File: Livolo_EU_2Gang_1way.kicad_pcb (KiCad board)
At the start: 2 copper layers, 43 x 43 mm, 54 parts, among them IC1 ATMEGA328P, U1 ATSHA204A, U2 NRF24L01, U3 MIC5205-3.3, U4 MCP16301, U5 AT25DF512C

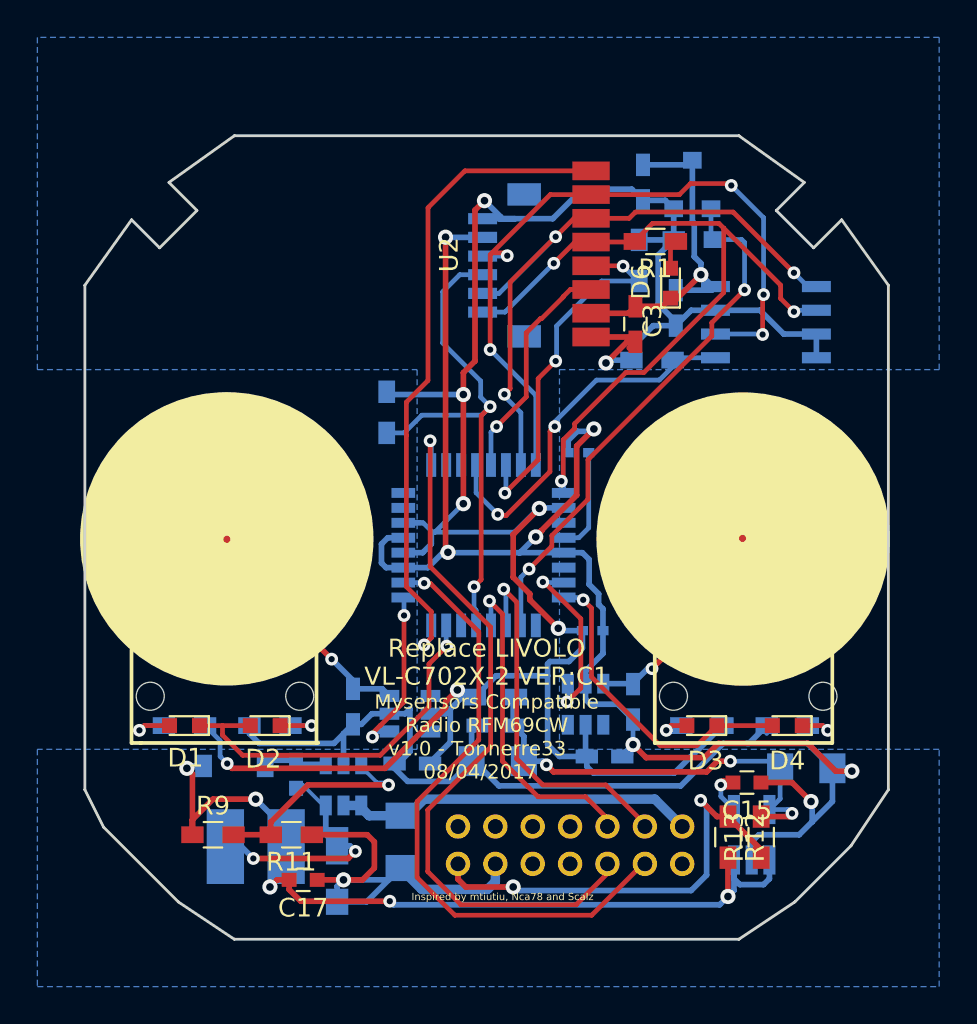
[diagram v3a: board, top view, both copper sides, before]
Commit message: replace TTP223 by MTCH105
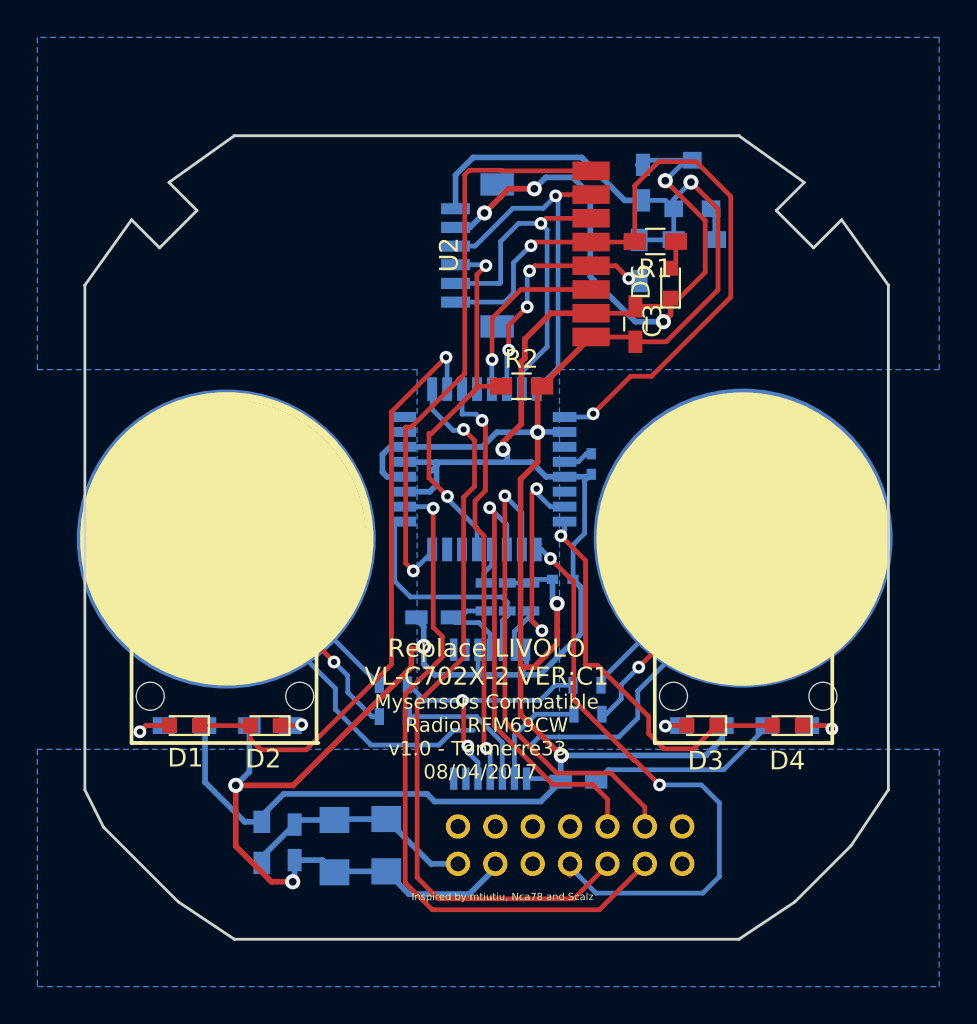
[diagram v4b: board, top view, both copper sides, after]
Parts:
- removed C11: 10u/25v, Livolo_EU_2Gang_1way:EIA3216
- removed C14, C7, C9: 100n, Capacitors_SMD:C_0603_HandSoldering
- removed C15: 470p, Capacitors_SMD:C_0603
- removed C16: 100n, Capacitors_SMD:C_0603
- removed C17: 22u, Capacitors_SMD:C_0603
- removed C8: 0-50pF, Capacitors_SMD:C_0603_HandSoldering
- removed D5: SS14M, Livolo:SS14M
- removed D7: 1N4148, Diodes_SMD:D_SOD-123
- removed L1: 15uH, Livolo:VLCF4020T-150MR68
- removed R10: 56k, Resistors_SMD:R_0603_HandSoldering
- removed R11: 10k, Resistors_SMD:R_0603_HandSoldering
- removed R12, R13: *1, Resistors_SMD:R_0603_HandSoldering
- removed R9: 31k6, Resistors_SMD:R_0603_HandSoldering
- removed U$1, U$5: SENSOR_PAD_ROUND, Livolo:touch_pad_16mm
- removed U$4, U$6: TTP223-BA6, TO_SOT_Packages_SMD:SOT-23-6
- removed U3: MIC5205-3.3, TO_SOT_Packages_SMD:SOT-23-5_HandSoldering
- removed U4: MCP16301, TO_SOT_Packages_SMD:SOT-23-6
- removed U5: AT25DF512C, Housings_SOIC:SOIC-8_3.9x4.9mm_Pitch1.27mm
- added C1: 100n, Capacitors_SMD:C_0603_HandSoldering, B.Cu at (153.4, 118.1)
- added R14: 4K7, Resistors_SMD:R_0603, B.Cu at (143.5, 114.6)
- added R15: 0, Resistors_SMD:R_0603, B.Cu at (143.5, 112.9)
- added R16: 4K7, Resistors_SMD:R_0603, B.Cu at (153.9, 114.5)
- added R17: 0, Resistors_SMD:R_0603, B.Cu at (153.9, 112.9)
- added R18: 10K, Resistors_SMD:R_0603, B.Cu at (150.9, 108.2)
- added R19: 10K, Resistors_SMD:R_0603, B.Cu at (148.4, 108.2)
- added R20: 10K, Resistors_SMD:R_0603, B.Cu at (149.6, 108.2)
- added U6: Touch, Livolo:livolo_ts_guard, B.Cu at (134.6, 105.1)
- added U7: Touch, Livolo:livolo_ts_guard, B.Cu at (162.2, 105.0)
- added U8: MTCH105, Housings_SSOP:SSOP-14_5.3x6.2mm_Pitch0.65mm, B.Cu at (148.7, 114.5)
- C4: value 0-50pF -> 1uF
- R2: moved to F.Cu
- moved C12 25.6 mm to (140.4, 121.5), turned to 90 degrees
- moved L2 14.7 mm to (136.5, 121.3), turned to 270 degrees
- moved C13 12.4 mm to (138.2, 121.3), turned to 270 degrees
- moved C4 11.6 mm to (145.7, 109.3), turned to 180 degrees
- moved C10 7.47 mm to (143.1, 121.5), turned to 90 degrees
- moved R2 7.35 mm to (150.4, 96.9), turned to 0 degrees
- moved IC1 4.06 mm to (148.4, 101.4)
- moved C6 3.18 mm to (152.6, 107.2)
- moved SL2 1.54 mm to (148.1, 89.9)
- moved C2 0.92 mm to (154.1, 101.1), turned to 90 degrees
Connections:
- C10 pad +: Net-(C10-Pad+) -> /3.3VCC-Liv
- C12 pad +: Net-(C10-Pad+) -> /3.3VCC-Liv
- C13 pad 1: Net-(C10-Pad+) -> /3.3VCC-Liv
- C4 pad 1: GND -> Net-(C4-Pad1)
- C4 pad 2: Net-(C4-Pad2) -> GND
- IC1 pad 10: (no net) -> /LED1
- IC1 pad 11: (no net) -> /MTPM
- IC1 pad 12: /FLASH_CS -> (no net)
- IC1 pad 25: (no net) -> /BUZZER
- IC1 pad 26: /A3_ATSHA -> /L2_SET
- IC1 pad 27: /L2_SET -> /L2_RST
- IC1 pad 28: /L2_RST -> /MTSA
- IC1 pad 31: /LED1 -> (no net)
- L2 pad 2: Net-(C10-Pad+) -> /3.3VCC-Liv
- U$2 pad 13: /+12VCC -> (no net)
- U$2 pad 8: (no net) -> /BUZZER
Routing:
- net /3.3VCC_1: track 49.1 -> 0.00 mm, vias 5 -> 0
- net GND: track 174.9 -> 134.8 mm, vias 9 -> 8
- net Net-(R15-Pad2): track 0.00 -> 33.6 mm
- net /BUZZER: track 0.00 -> 32.8 mm, vias 0 -> 2
- net Net-(R17-Pad2): track 0.00 -> 31.9 mm
- net /A3_ATSHA: track 28.8 -> 1.73 mm, vias 2 -> 0
- net Net-(C10-Pad+): track 24.5 -> 0.00 mm, vias 3 -> 0
- net /MTPM: track 0.00 -> 22.4 mm, vias 0 -> 2
- net /+12VCC: track 20.5 -> 0.00 mm
- net /MISO: track 40.5 -> 20.2 mm, vias 5 -> 1
- net /FLASH_CS: track 19.9 -> 0.00 mm, vias 2 -> 0
- net VCC: track 135.7 -> 118.1 mm, vias 8 -> 4
- net /MOSI: track 35.0 -> 20.5 mm, vias 3 -> 1
- net Net-(R15-Pad1): track 0.00 -> 14.1 mm, vias 0 -> 2
- net Net-(R14-Pad2): track 0.00 -> 13.1 mm, vias 0 -> 1
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
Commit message: ajust silkscreen
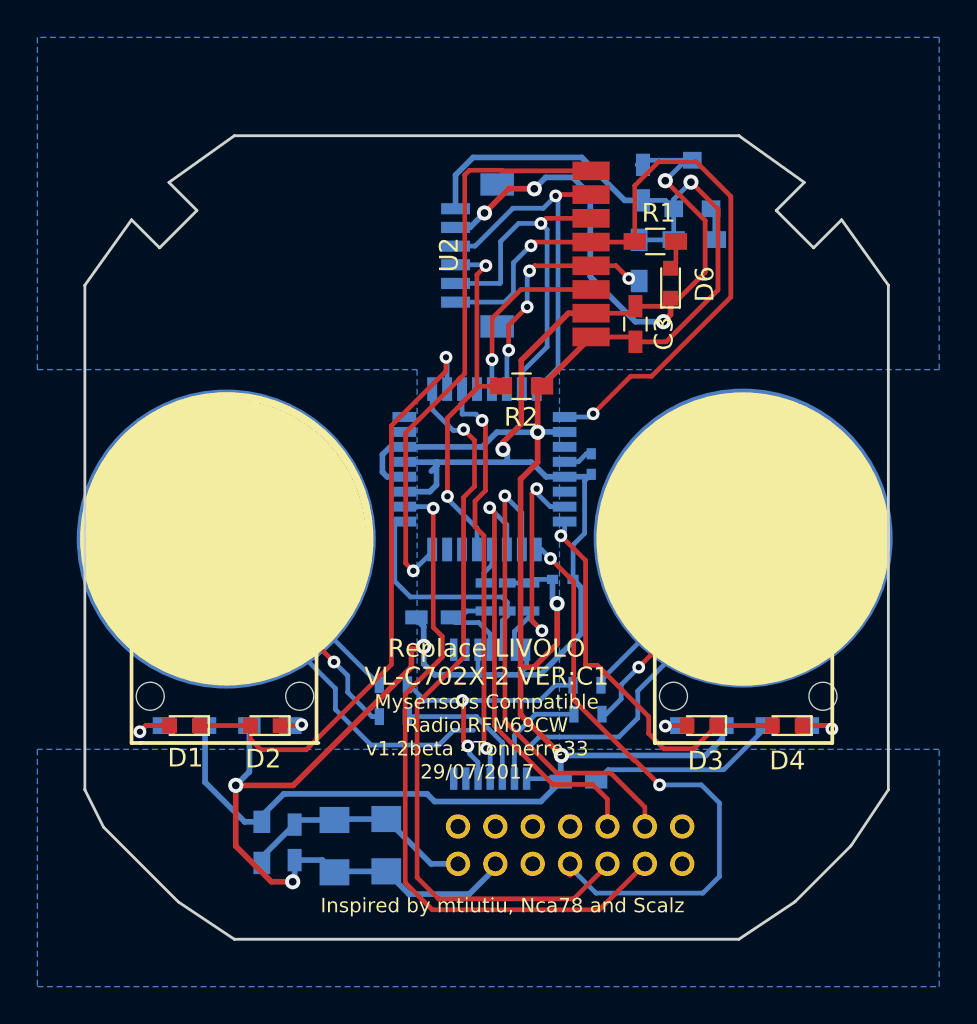
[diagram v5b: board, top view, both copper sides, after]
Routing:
- net /RST: track 21.0 -> 20.1 mm
- net GND: track 134.8 -> 134.3 mm
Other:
- board text added: "v1.2beta - Tonnerre33 29/07/2017"
- board text removed: "v1.0 - Tonnerre33 08/04/2017"

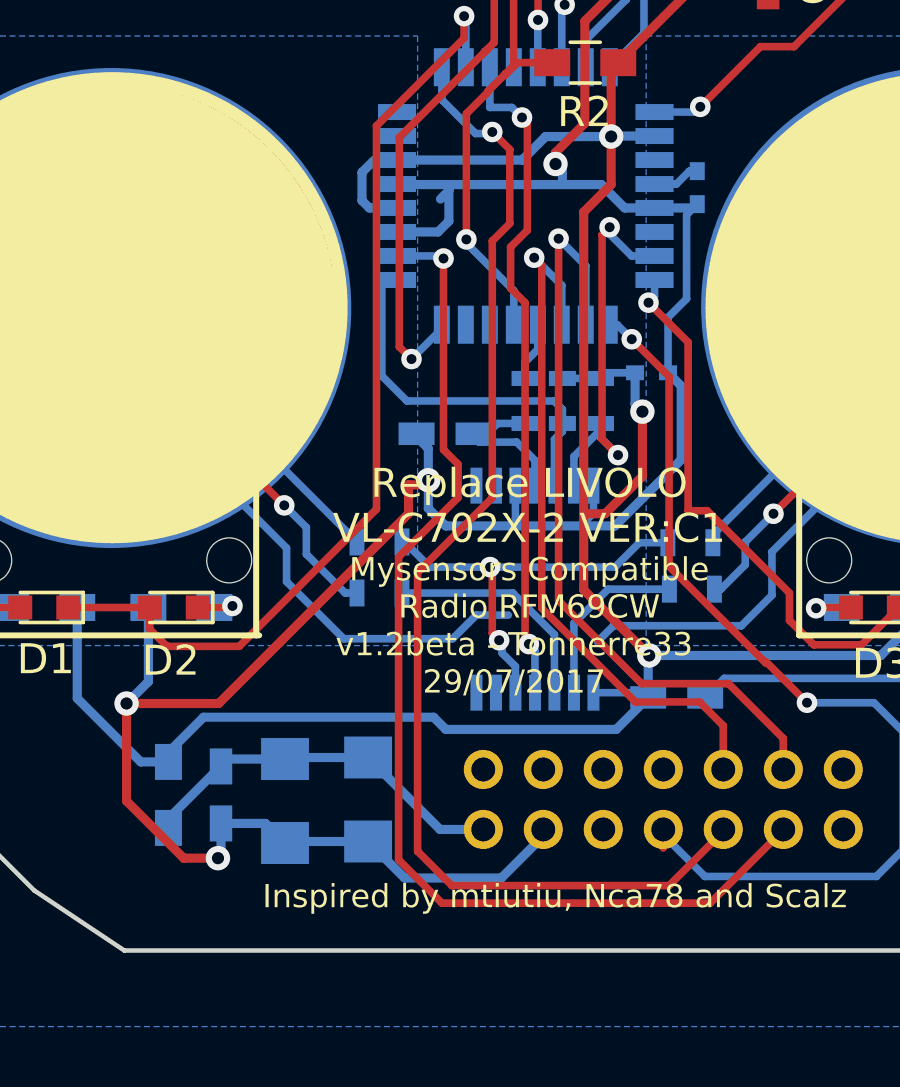
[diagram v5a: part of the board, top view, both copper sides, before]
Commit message: adding shunt for test with or without guard
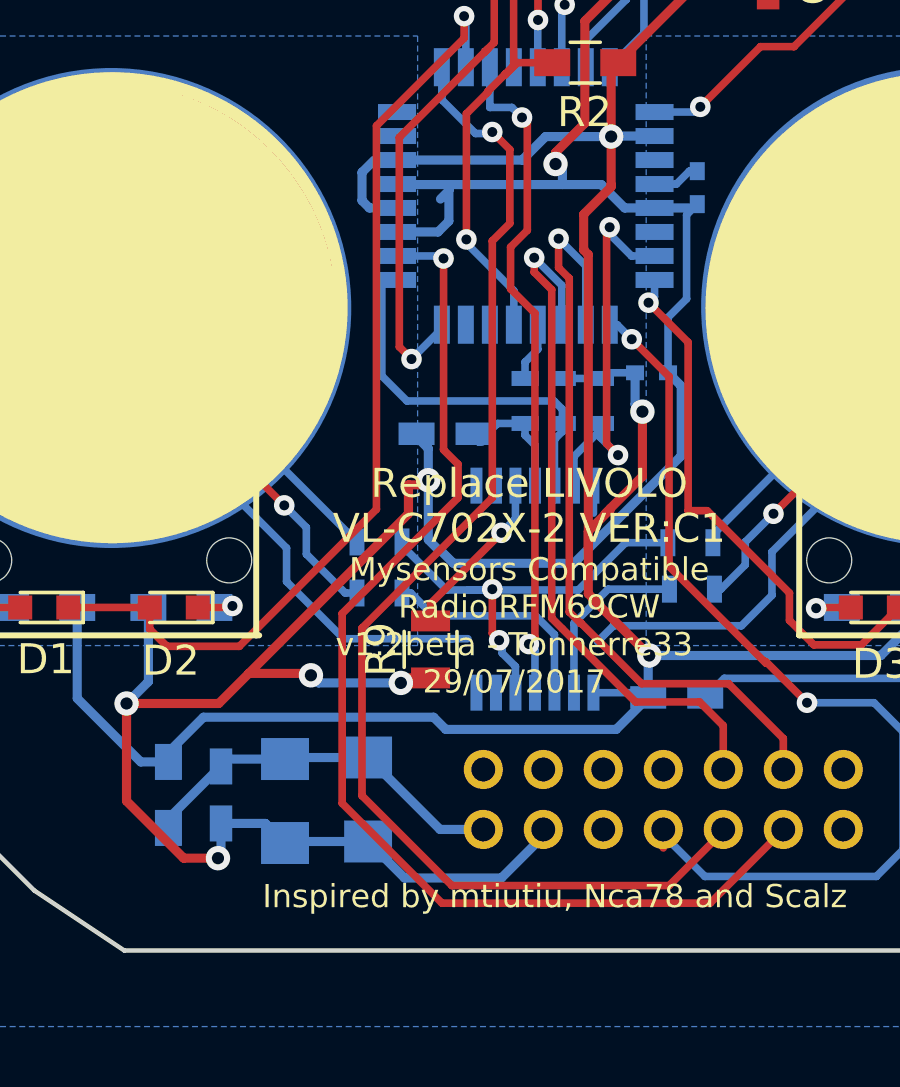
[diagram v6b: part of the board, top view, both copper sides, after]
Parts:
- added R9: 0*, Resistors_SMD:R_0805, F.Cu at (145.2, 116.5)
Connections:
- U8 pad 10: GND -> Net-(R9-Pad2)
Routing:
- net GND: track 134.3 -> 140.0 mm, vias 8 -> 10
- net Net-(R9-Pad2): track 0.00 -> 5.68 mm, vias 0 -> 1
- net Net-(R15-Pad2): track 33.6 -> 32.0 mm
- net /L1_RST: track 37.1 -> 38.7 mm
- net /L1_SET: track 40.2 -> 41.8 mm
- net VCC: track 118.1 -> 119.0 mm
- net Net-(R15-Pad1): track 14.1 -> 14.9 mm
- net Net-(C4-Pad1): track 4.87 -> 4.11 mm

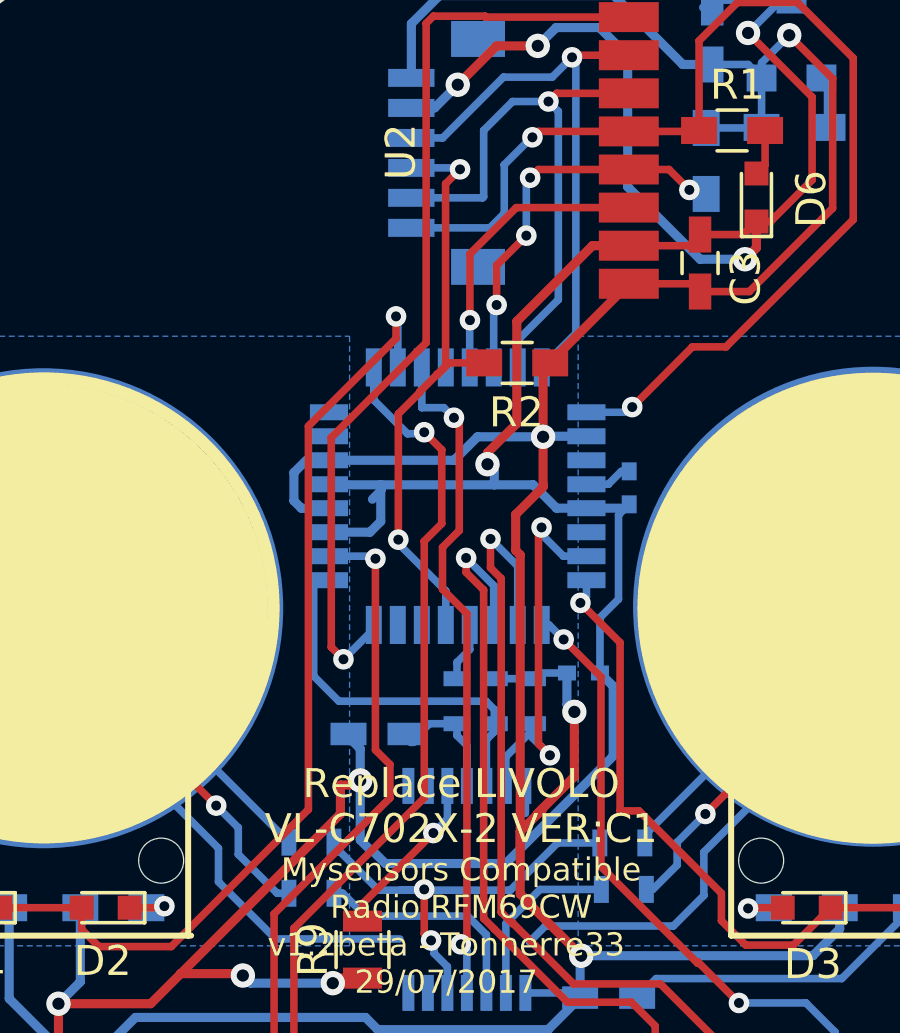
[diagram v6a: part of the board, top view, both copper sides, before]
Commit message: moving C6 for be closer of pin 4 and 5
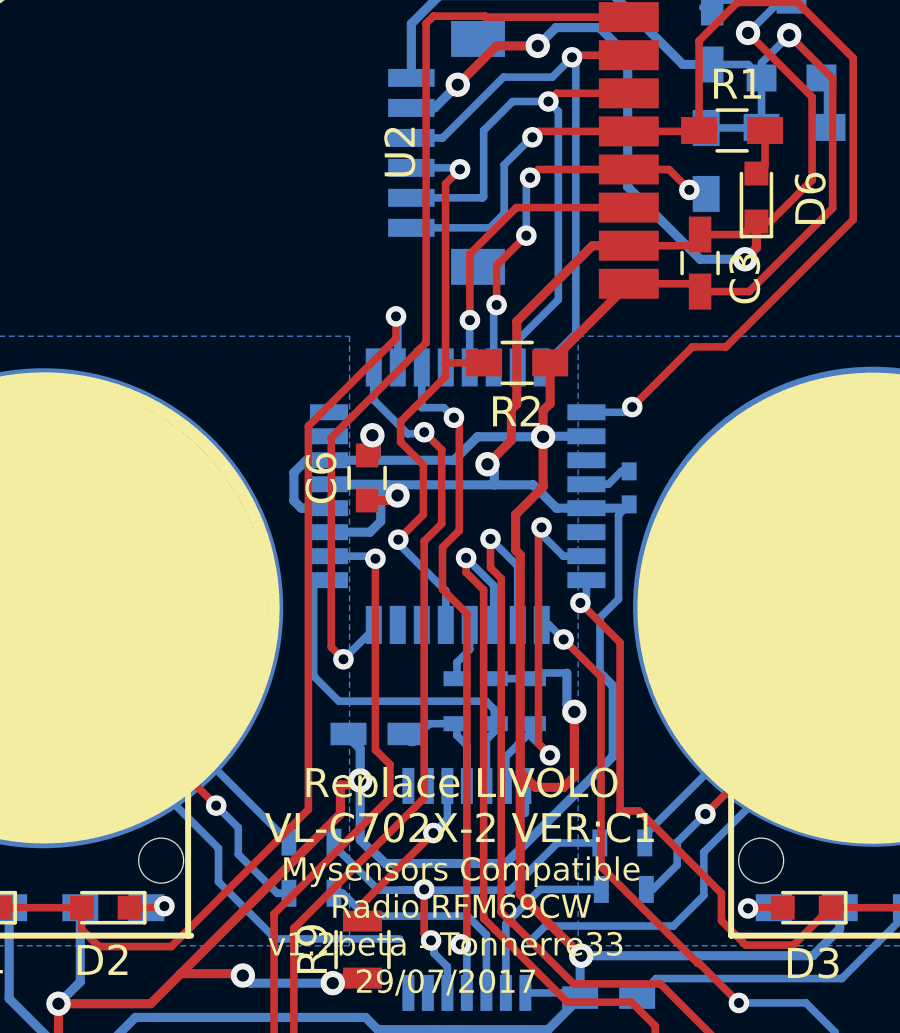
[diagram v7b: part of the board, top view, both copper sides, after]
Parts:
- C6: footprint Capacitors_SMD:C_0402 -> Capacitors_SMD:C_0603; moved to F.Cu
- moved C6 9.71 mm to (145.4, 100.7), turned to 90 degrees
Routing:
- net GND: track 140.0 -> 143.6 mm, vias 10 -> 11
- net VCC: track 119.0 -> 119.8 mm, vias 4 -> 5
